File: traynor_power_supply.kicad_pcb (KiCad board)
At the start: 2 copper layers, 102 x 47.5 mm, 32 parts, among them J1 AC IN, J10 OUT2, J11 OUT3, J2 AC IN, J3 Chassis GND, J4 OUT1, J5 TREM, J6 SW, J7 SW, J8 CHOKE, J9 CHOKE

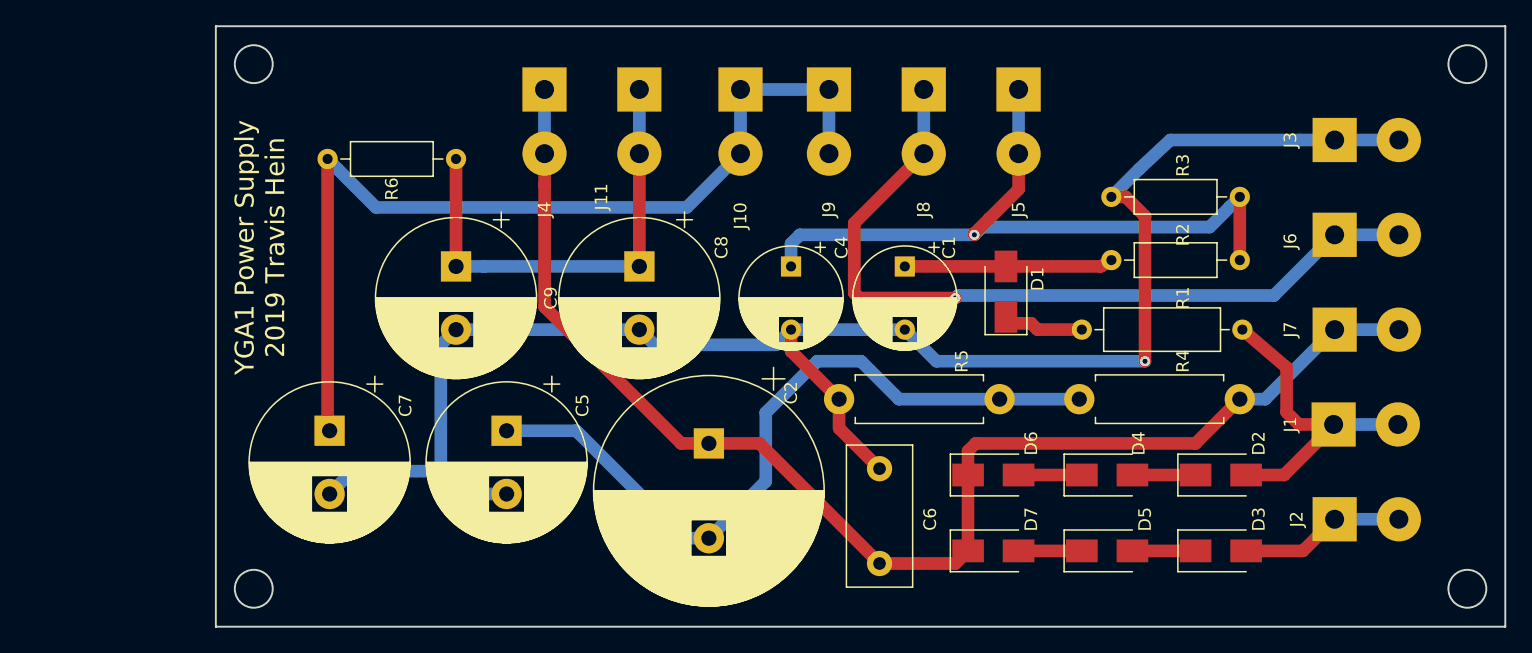
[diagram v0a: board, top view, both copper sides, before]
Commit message: change the 100uF capacitor to be 2 47uF capacitors
find there was a capacitor without a footprint on the schematic too, so we were missing it before.
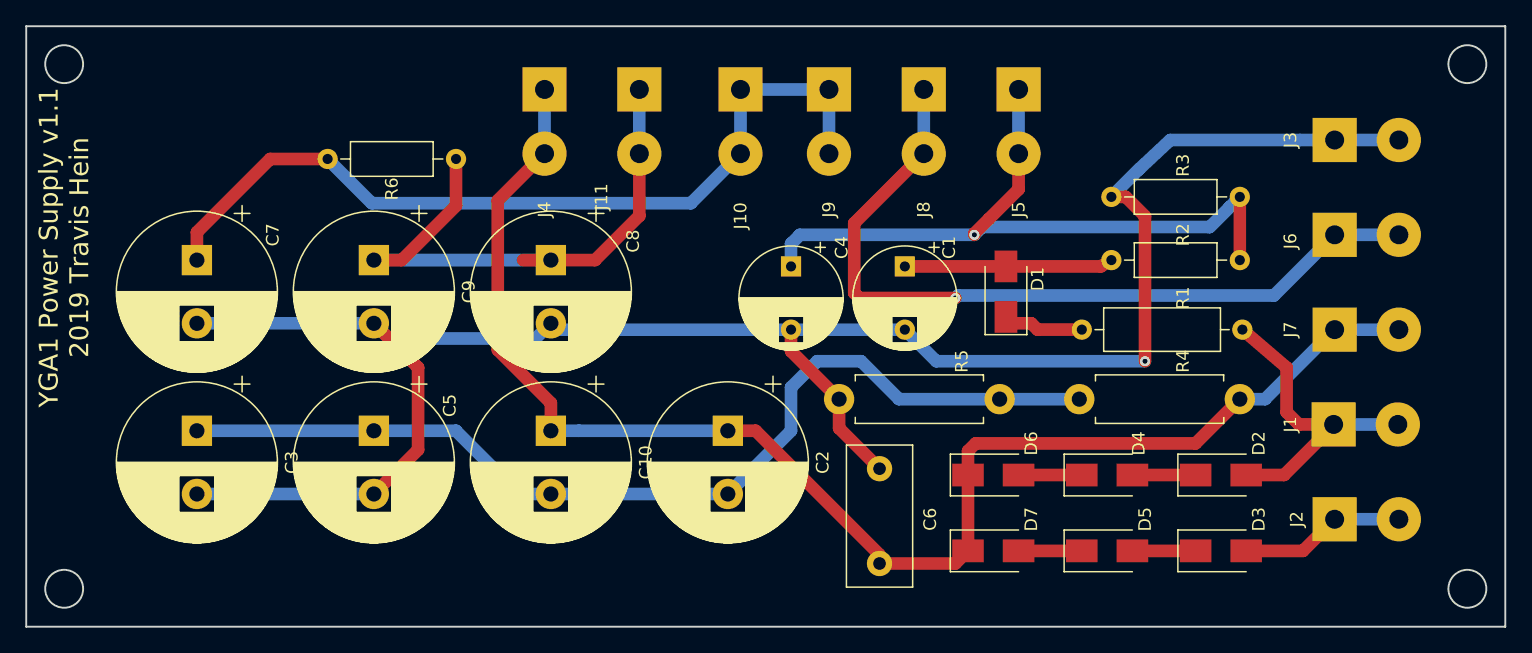
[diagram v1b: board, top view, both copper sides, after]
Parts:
- added C10: 47uF 450V, Capacitor_THT:CP_Radial_D12.5mm_P5.00mm, F.Cu at (91.5, 114.5)
- added C3: 47uF 450V, Capacitor_THT:CP_Radial_D12.5mm_P5.00mm, F.Cu at (63.5, 114.5)
- C2: value 100uF 450V -> 47uF 450V; footprint Capacitor_THT:CP_Radial_D18.0mm_P7.50mm -> Capacitor_THT:CP_Radial_D12.5mm_P5.00mm
- C9: value 47uF 450V -> 10uF 450V
- moved C7 17.1 mm to (63.5, 101.0)
- moved C5 10.5 mm to (77.5, 114.5)
- moved C8 7.02 mm to (91.5, 101.0)
- moved C9 6.52 mm to (77.5, 101.0)
- moved C2 1.80 mm to (105.5, 114.5)
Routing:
- net Net-(C1-Pad2): track 136.9 -> 160.9 mm
- net Net-(C10-Pad2): track 59.0 -> 79.5 mm
- net Net-(C8-Pad1): track 37.0 -> 46.6 mm
- net Net-(C10-Pad1): track 105.5 -> 114.4 mm
- net Net-(C7-Pad1): track 74.7 -> 67.8 mm
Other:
- board size 102 x 47.5 mm -> 117 x 47.5 mm
- board text added: "YGA1 Power Supply v1.1 2019 Travis Hein"
- board text removed: "YGA1 Power Supply 2019 Travis Hein"
